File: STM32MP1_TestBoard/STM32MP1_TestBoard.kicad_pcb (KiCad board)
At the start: 4 copper layers, 73.7 x 80 mm, 102 parts, among them J1 Conn_01x27, J12 Micro_SD_Card, J13 Micro_SD_Card, J14 USB_B_Micro, J2 Conn_01x27, J3 Conn_01x27, J4 Conn_01x27, J5 Conn_02x03_Odd_Even, J6 Conn_02x05_Odd_Even, J7 Conn_01x06, J8 USB_B_Micro, J9 Barrel_Jack, Q1 DMG2302U, SW2 SW_SPST, U1 STM32MP157xAB, U2 MT41K256M16TW-107, U3 SE8233X2, U4 TPS54202DDC

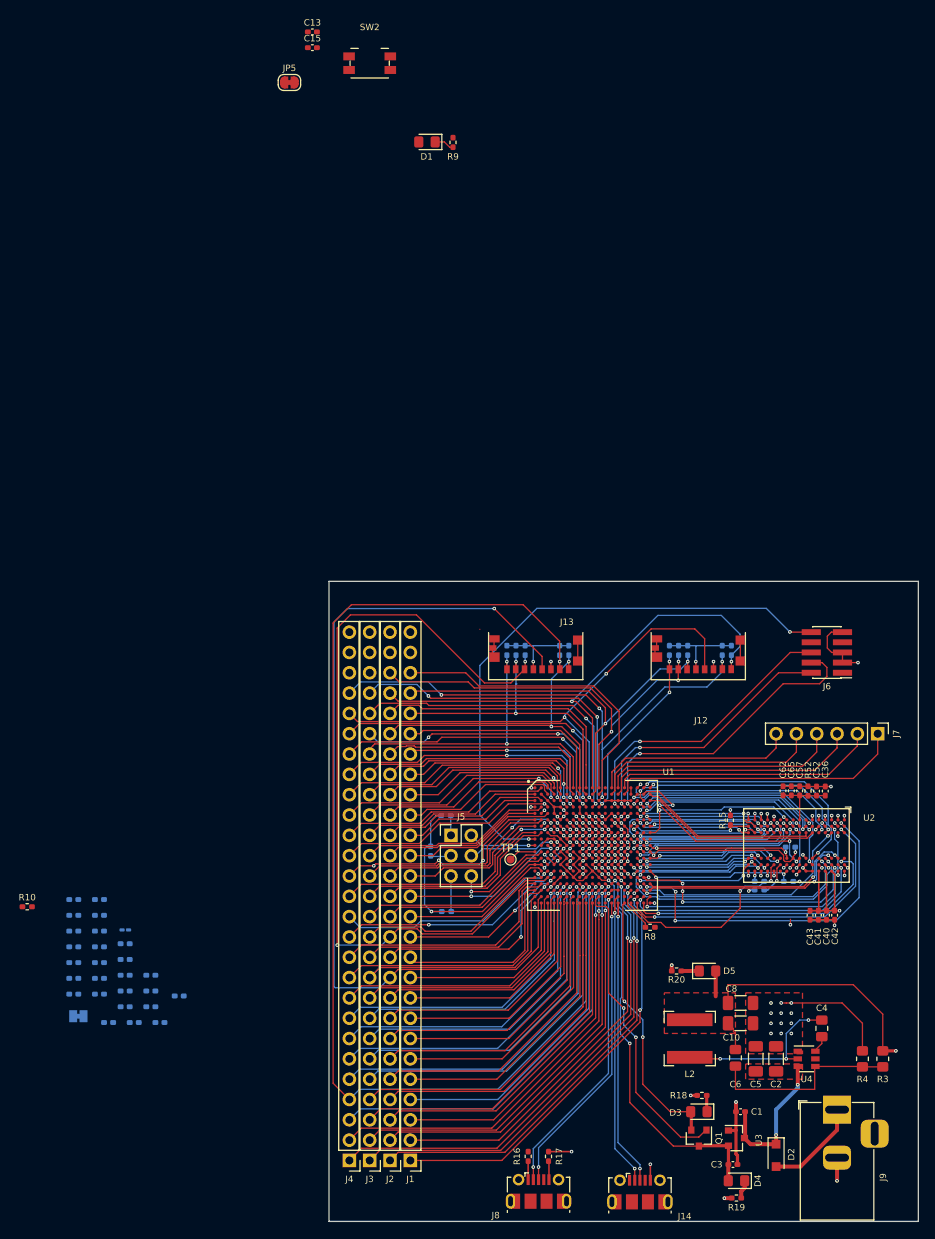
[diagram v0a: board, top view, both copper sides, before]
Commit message: finished RevA draft layout
- Added MPU bypass caps
- length tuned DDR3L traces
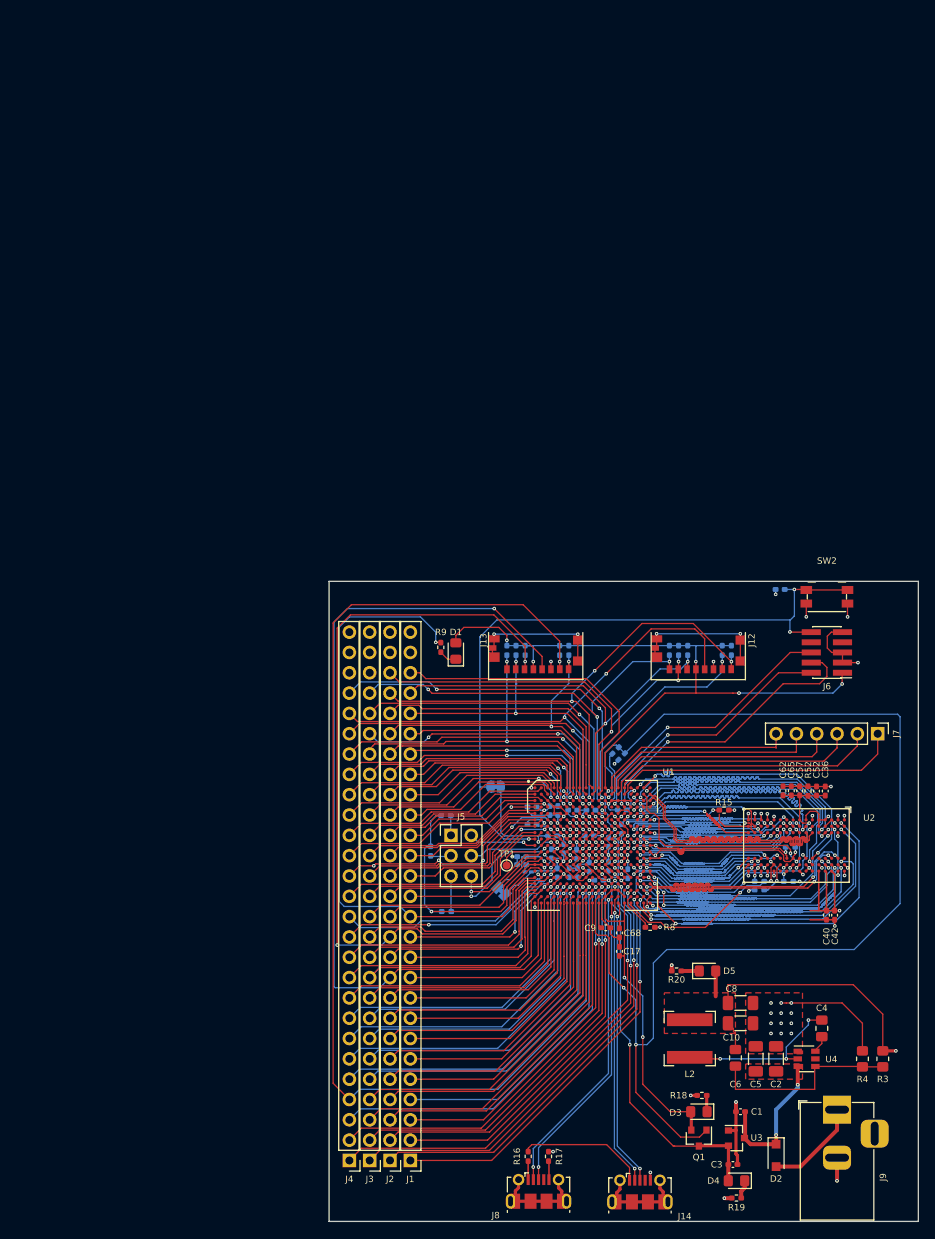
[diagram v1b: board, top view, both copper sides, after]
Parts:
- removed C41, C43: 100nF, Capacitor_SMD:C_0402_1005Metric_Pad0.74x0.62mm_HandSolder
- C13, C15, JP5, R10: moved to B.Cu
- C17, C68, C9: moved to F.Cu
- moved C15 103.0 mm to (154.9, 101.7)
- moved JP5 91.7 mm to (147.8, 95.5)
- moved C13 91.0 mm to (183.4, 70.9), turned to 180 degrees
- moved SW2 87.8 mm to (189.2, 71.8)
- moved R10 74.9 mm to (163.6, 100.8), turned to 270 degrees
- moved C69 69.5 mm to (163.6, 98.4)
- moved C7 67.7 mm to (163.6, 91.8), turned to 225 degrees
- moved C23 65.0 mm to (164.3, 106.4), turned to 270 degrees
- moved C22 64.9 mm to (159.7, 98.5), turned to 180 degrees
- moved C70 64.5 mm to (162.8, 91.0), turned to 225 degrees
- moved C17 64.5 mm to (163.3, 116.1), turned to 90 degrees
- moved C19 64.0 mm to (160.7, 107.2), turned to 180 degrees
- moved D1 63.7 mm to (142.8, 78.6), turned to 90 degrees
- moved C24 63.6 mm to (158.0, 106.3), turned to 270 degrees
- moved C29 63.6 mm to (157.9, 104.0), turned to 270 degrees
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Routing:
- net /PSU/1V8_DETECT: track 39.0 -> 154.6 mm, vias 2 -> 3
- net /DebugInterface1/3.3V_VDD: track 127.4 -> 214.2 mm, vias 8 -> 13
- net /GPIO/BOOT_STATUS: track 19.1 -> 79.8 mm, vias 0 -> 1
- net GNDS: track 154.2 -> 195.4 mm, vias 117 -> 109
- net /PSU/1.35V_VDDCORE: track 111.5 -> 129.2 mm, vias 57 -> 52
- net +5V: track 0.00 -> 16.1 mm
- net /DebugInterface1/NRST: track 72.4 -> 87.5 mm, vias 2 -> 3
- net /DDR/DDR_DQ11: track 34.5 -> 48.9 mm
- net /DDR/DDR_DQ14: track 31.2 -> 45.1 mm
- net Net-(C15-Pad1): track 0.00 -> 13.5 mm, vias 0 -> 1
- net /DDR/DDR_DQS0_P: track 22.5 -> 34.9 mm
- net /DDR/DDR_DQS0_N: track 22.1 -> 34.4 mm
- net Net-(J8-Pad6): track 0.00 -> 12.1 mm
- net /DDR/DDR_DQ6: track 23.2 -> 35.2 mm
- net Net-(J12-Pad9): track 5.07 -> 17.0 mm, vias 0 -> 2
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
